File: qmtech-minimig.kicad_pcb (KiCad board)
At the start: 4 copper layers, 142.3 x 105.7 mm, 150 parts, among them IC1 ESP32-WROVER-B_(16MB), J1 DB9_Male, J10 DB23_Female_MountingHoles, J11 Conn_01x03_Male, J2 DB9_Male, J3 SCHA5B0200, J4 10118193-0001LF, J5 AUDIO-CONNECTOR-6P-SMD-344003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, J6 Mini-DIN-6, J7 Conn_02x13_Odd_Even, J8 Conn_01x04, J9 47151-0001, Q1 MMBT2222A, Q2 MMBT2222A, Q3 BSS84, SW1 SW_Push, U2 QM_XC7A35T_DDR3, U3 LT1963AxST-1.8, U4 INTERFACE-CP2102-GMR(QFN28), U5 MT3608, U6 TXS0108EPWR, U7 TXS0108EPWR

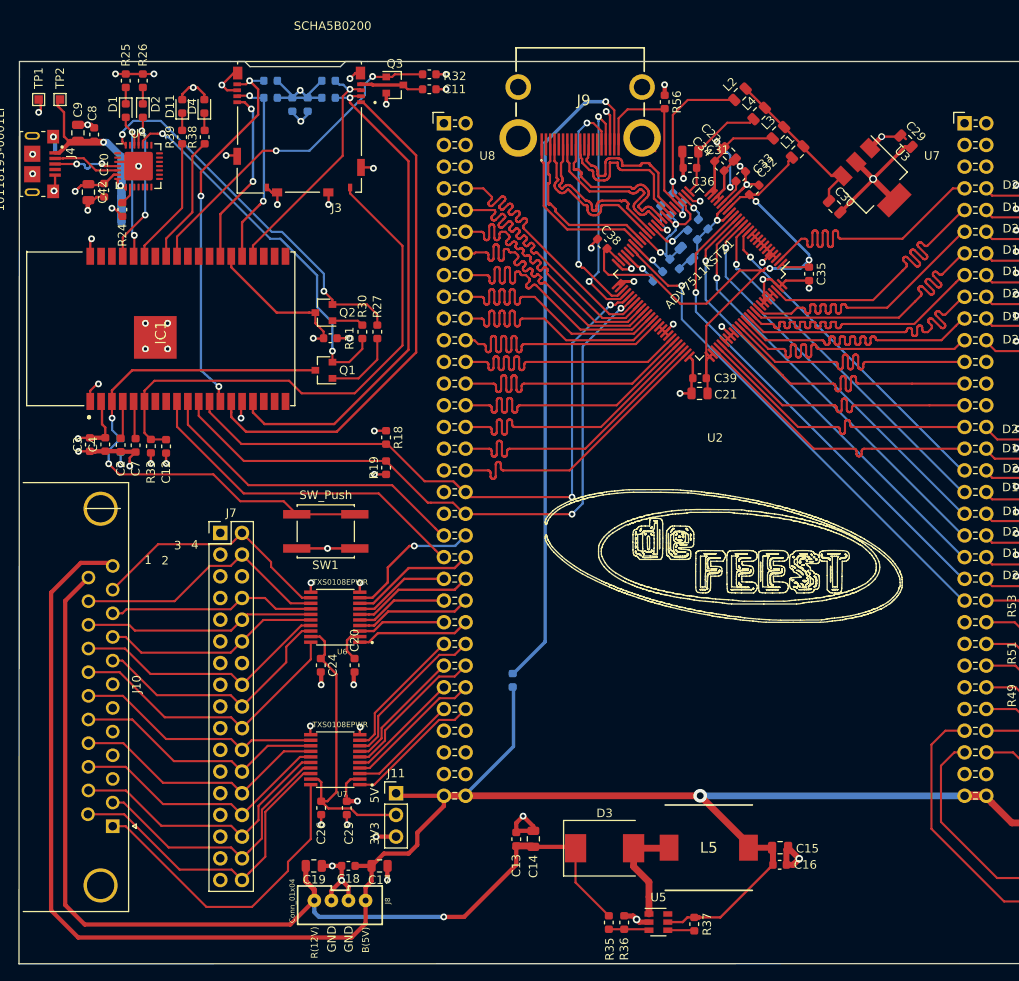
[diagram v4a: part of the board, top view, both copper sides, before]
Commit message: Fixed HDMI Impedance to 50Ohm, 100Ohm differential, for 0.1mm bord. Add pullups to HDMI I2C, connected DE pin to FPGA.
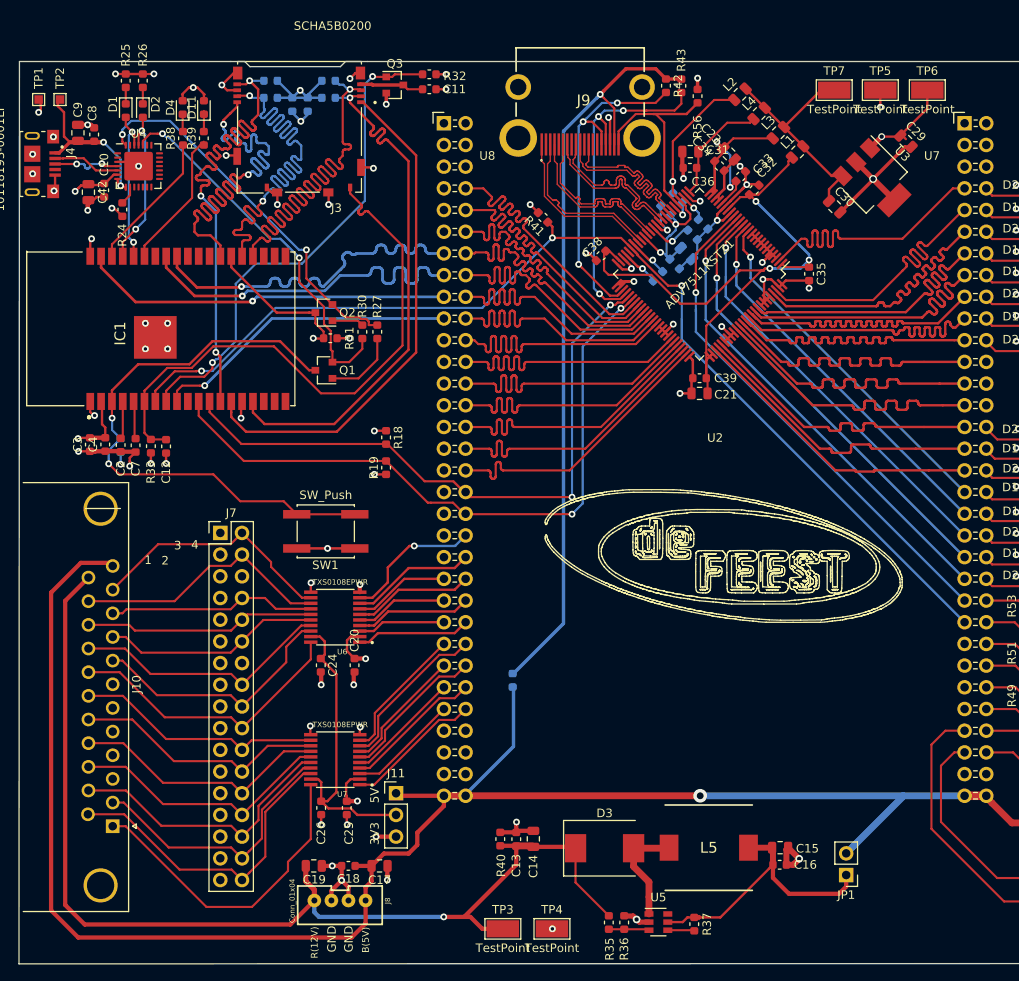
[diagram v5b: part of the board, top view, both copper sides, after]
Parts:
- added JP1: Jumper, Connector_PinHeader_2.54mm:PinHeader_1x02_P2.54mm_Vertical, F.Cu at (156.4, 140.5)
- added R40: 1M, Resistor_SMD:R_0603_1608Metric, F.Cu at (116.0, 136.3)
- added R41: 2K, Resistor_SMD:R_0603_1608Metric, F.Cu at (121.0, 63.5)
- added R42: 2k, Resistor_SMD:R_0603_1608Metric, F.Cu at (135.3, 48.1)
- added R43: 2k, Resistor_SMD:R_0603_1608Metric, F.Cu at (137.2, 48.1)
- added TP3: TestPoint, TestPoint:TestPoint_Keystone_5019_Minature, F.Cu at (116.2, 146.8)
- added TP4: TestPoint, TestPoint:TestPoint_Keystone_5019_Minature, F.Cu at (122.0, 146.8)
- added TP5: TestPoint, TestPoint:TestPoint_Keystone_5019_Minature, F.Cu at (160.4, 48.6)
- added TP6: TestPoint, TestPoint:TestPoint_Keystone_5019_Minature, F.Cu at (165.9, 48.6)
- added TP7: TestPoint, TestPoint:TestPoint_Keystone_5019_Minature, F.Cu at (155.1, 48.6)
- moved R56 3.91 mm to (139.1, 49.3)
- moved R38 2.54 mm to (78.8, 54.2)
- moved R39 2.54 mm to (81.2, 54.2)
- moved D11 2.54 mm to (81.2, 50.6)
- moved D4 2.54 mm to (78.8, 50.6)
- moved C38 1.41 mm to (127.8, 68.0), turned to 45 degrees
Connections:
- net STM_SPI1_CS renamed Net-(U2-PadU729)
- net STM_SPI1_MISO renamed Net-(U2-PadU723)
- net STM_SPI1_MOSI renamed Net-(U2-PadU721)
- net STM_SPI1_NSS renamed Net-(U2-PadU727)
- net STM_SPI1_SCK renamed Net-(U2-PadU725)
- net STM_USART1_CTS renamed Net-(U2-PadU79)
- net STM_USART1_RTS renamed Net-(U2-PadU77)
- net STM_USART1_RX renamed Net-(U2-PadU711)
- ADV7511KSTZ1 pad 97: GND -> ADV_DE
- C15 pad 1: VIN5V -> Net-(C15-Pad1)
- C16 pad 1: VIN5V -> Net-(C15-Pad1)
- IC1 pad 10: ESP_UART1_RX -> Net-(IC1-Pad10)
- IC1 pad 29: ADV_INT -> Net-(IC1-Pad29)
- IC1 pad 30: ESP_SD_VCC_EN -> ESP_VSPI_CLK
- IC1 pad 31: /MCU/LED1 -> ESP_VSPI_MISO
- IC1 pad 36: Net-(IC1-Pad36) -> /MCU/LED1
- IC1 pad 37: Net-(IC1-Pad37) -> ESP_VSPI_MOSI
- IC1 pad 7: Net-(IC1-Pad7) -> ADV_INT
- IC1 pad 8: Net-(IC1-Pad8) -> ESP_SD_VCC_EN
- IC1 pad 9: ESP_UART1_TX -> ESP_VSPI_CS
- L5 pad 2: VIN5V -> Net-(C15-Pad1)
- R37 pad 1: VIN5V -> Net-(C15-Pad1)
- U2 pad U713: STM_USART1_TX -> ESP_VSPI_CLK
- U2 pad U715: STM_USART1_CK -> ESP_VSPI_MISO
- U2 pad U717: STM_IO_34 -> ESP_VSPI_MOSI
- U2 pad U719: STM_IO_33 -> ESP_VSPI_CS
- U2 pad U739: ESP_UART1_RX -> Net-(U2-PadU739)
- U2 pad U741: ESP_UART1_TX -> Net-(U2-PadU741)
- U2 pad U811: ADV_B_0 -> ADV_DE
- U2 pad U813: ADV_B_1 -> ADV_B_0
- U2 pad U815: ADV_B_2 -> ADV_B_1
- U2 pad U817: ADV_B_3 -> ADV_B_2
- U2 pad U819: ADV_B_4 -> ADV_B_3
- U2 pad U821: ADV_B_5 -> ADV_B_4
- U2 pad U823: ADV_B_6 -> ADV_B_5
- U2 pad U825: ADV_B_7 -> ADV_B_6
- U2 pad U827: ADV_G_0 -> ADV_B_7
- U2 pad U829: ADV_CLK -> ADV_G_0
- U2 pad U831: ADV_G_1 -> ADV_CLK
- U2 pad U833: ADV_I2S0 -> ADV_G_1
- U2 pad U835: ADV_I2S1 -> ADV_I2S0
- U2 pad U837: ADV_I2S2 -> ADV_I2S1
- U2 pad U839: ADV_I2S3 -> ADV_I2S2
- U2 pad U841: ADV_SCLK -> ADV_I2S3
- U2 pad U843: ADV_LRCLK -> ADV_SCLK
- U2 pad U845: ADV_INT -> ADV_LRCLK
- U2 pad U847: Net-(U2-PadU847) -> ADV_INT
- U5 pad 5: VIN5V -> Net-(C15-Pad1)
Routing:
- net GND: track 262.6 -> 358.3 mm, vias 84 -> 86
- net ADV_INT: track 58.2 -> 127.9 mm, vias 1 -> 3
- net 3V3: track 124.7 -> 175.6 mm, vias 41 -> 43
- net ESP_VSPI_MOSI: track 0.00 -> 43.4 mm, vias 0 -> 1
- net ESP_VSPI_MISO: track 0.00 -> 43.1 mm, vias 0 -> 1
- net ESP_VSPI_CLK: track 0.00 -> 43.1 mm, vias 0 -> 1
- net ESP_SD_DATA0: track 22.9 -> 63.3 mm
- net ESP_UART1_TX: track 40.4 -> 0.00 mm
- net ESP_SD_DATA1: track 20.9 -> 60.0 mm
- net ESP_UART1_RX: track 37.9 -> 0.00 mm
- net ESP_VSPI_CS: track 0.00 -> 36.0 mm, vias 0 -> 1
- net ESP_SD_CMD: track 27.7 -> 63.5 mm
- net ADV_DE: track 0.00 -> 35.1 mm
- net Net-(C15-Pad1): track 0.00 -> 32.9 mm
- net ESP_SD_VCC_EN: track 39.7 -> 60.3 mm
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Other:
- net class HDMI: clearance 0.15 -> 0.2; trace_width 0.28 -> 0.16
- net class SPI_TOP added: clearance 0.15, trace_width 0.32, via_dia 0.8, via_drill 0.32

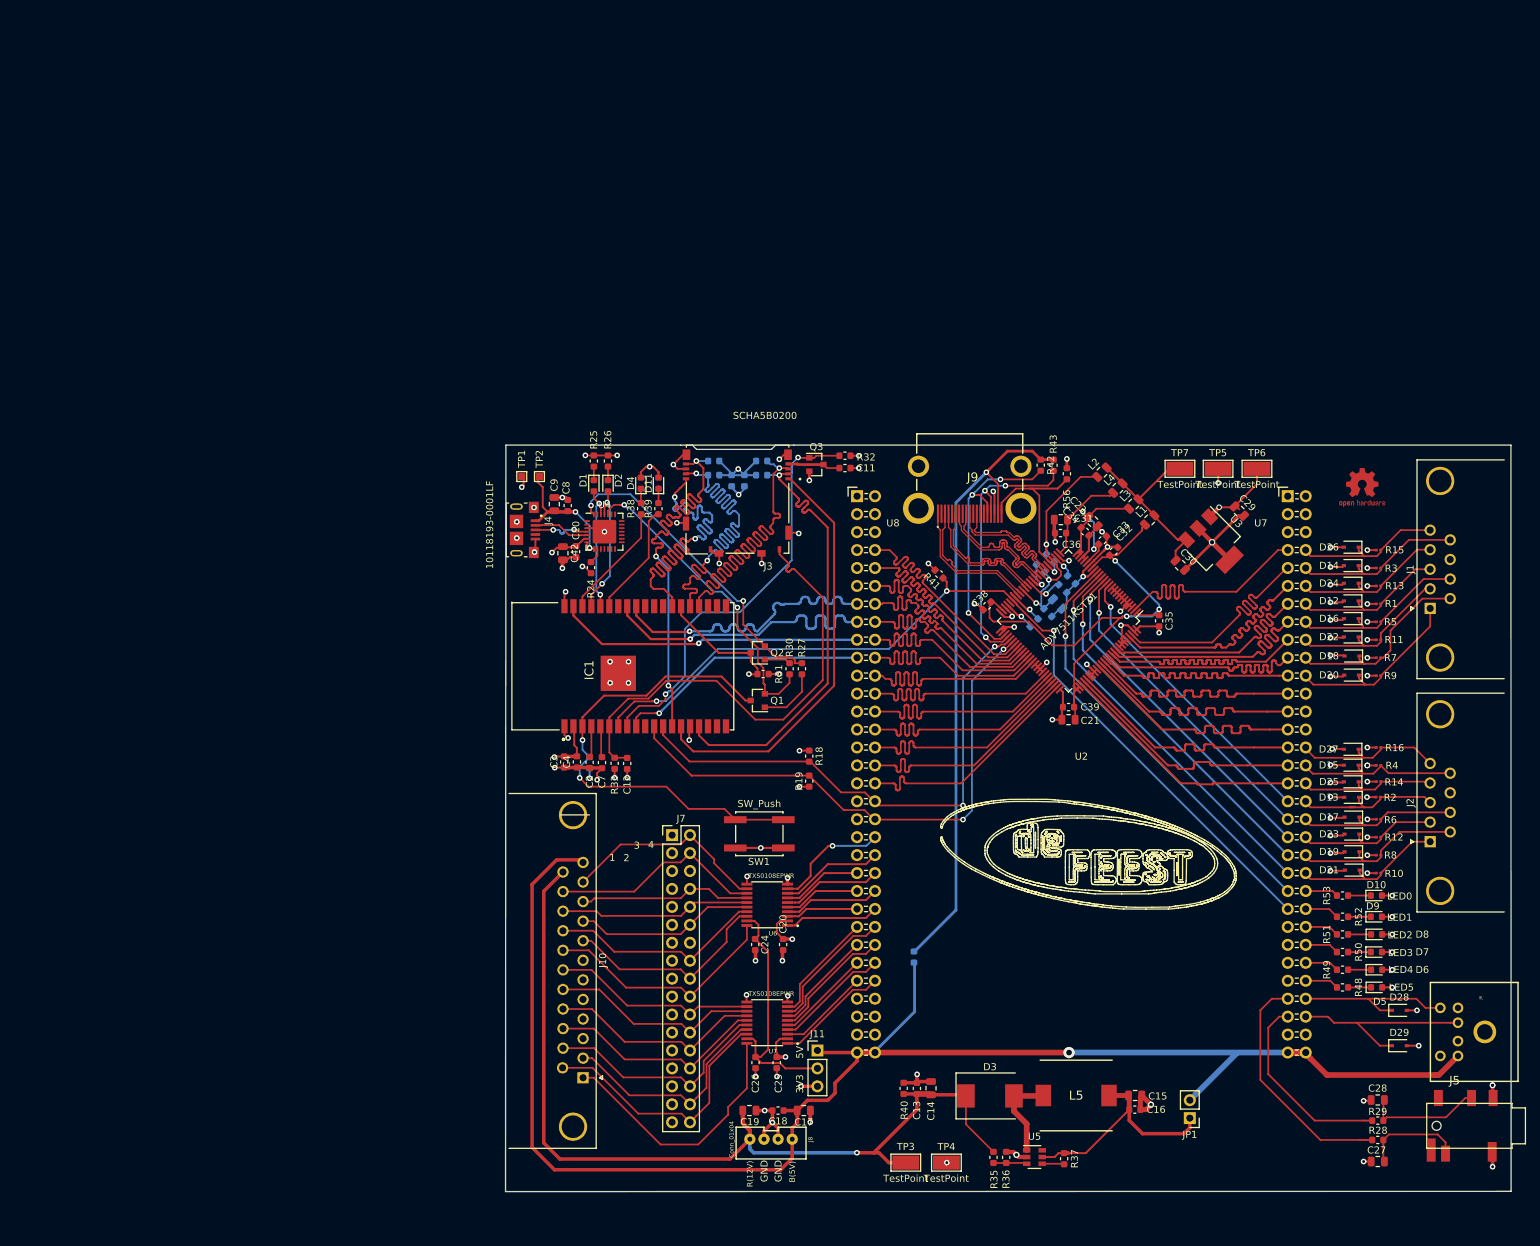
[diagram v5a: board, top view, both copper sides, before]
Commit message: Fixed some issues with the 50 Ohm impedance of the SPI lines. Added pinout .odt.
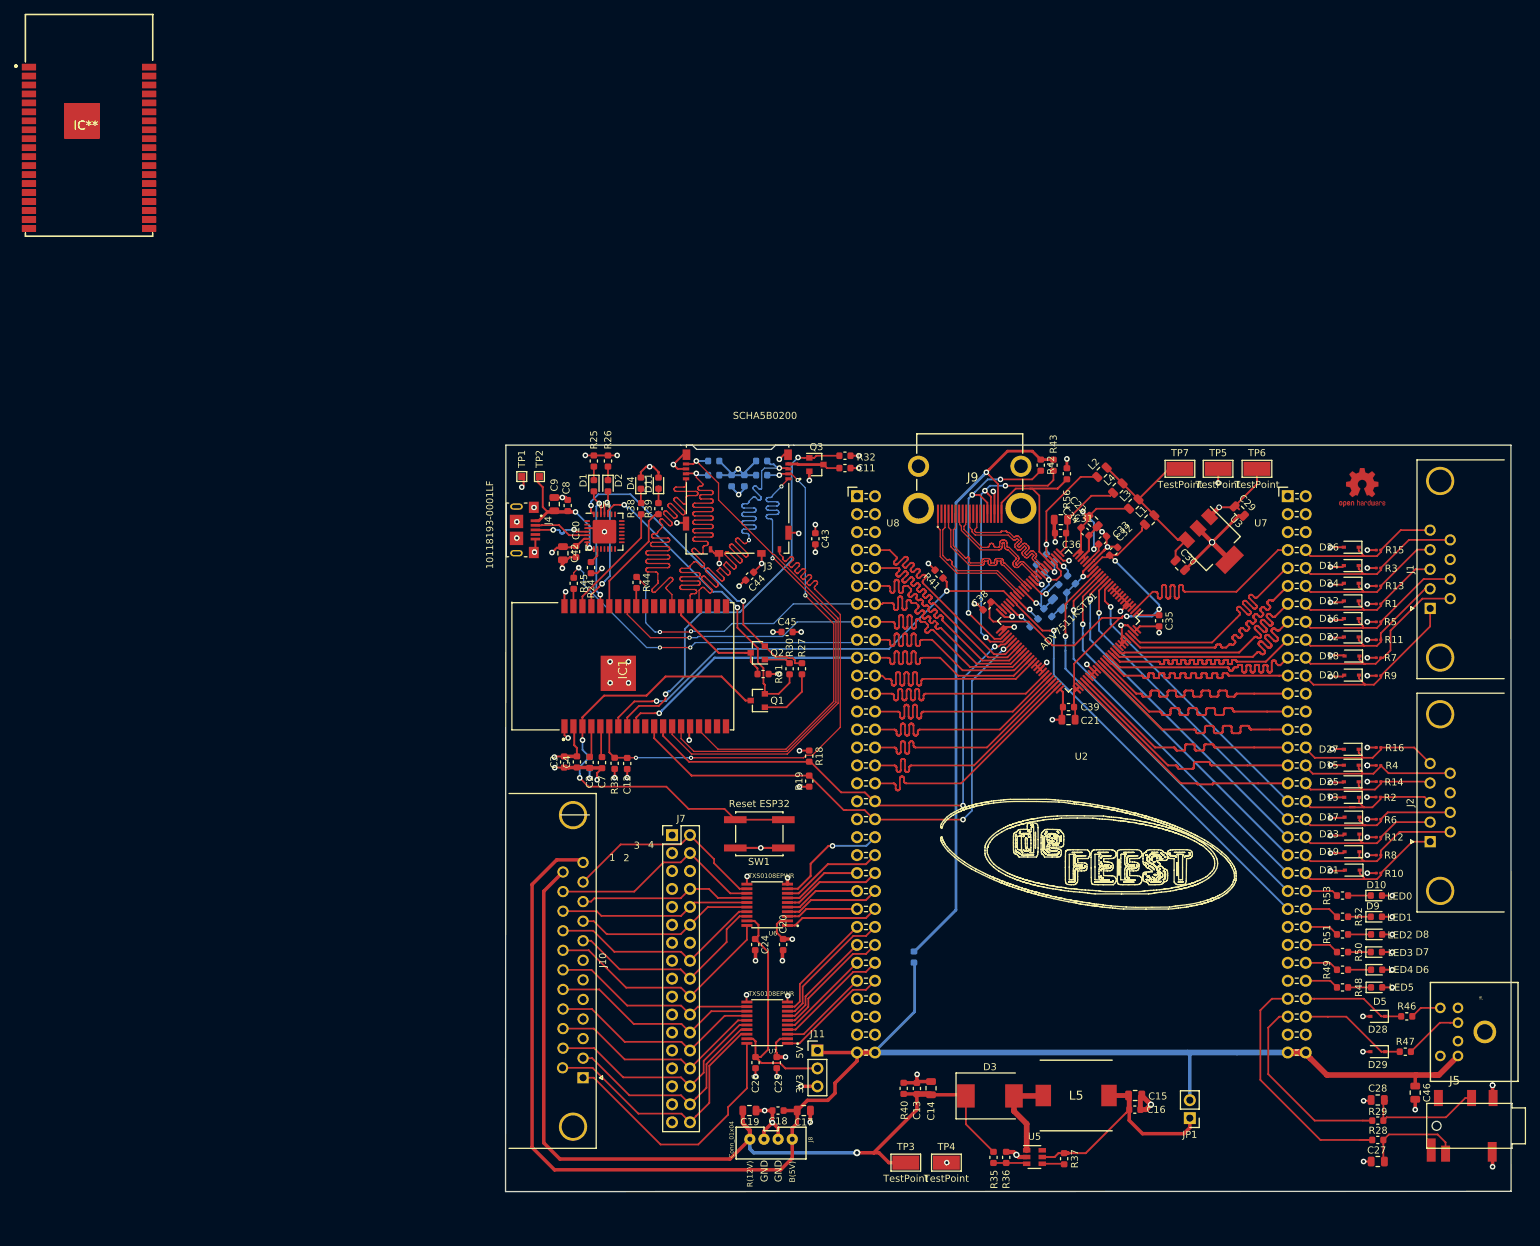
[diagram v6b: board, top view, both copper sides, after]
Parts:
- added C43: 10nF, Capacitor_SMD:C_0603_1608Metric, F.Cu at (103.5, 58.5)
- added C44: 10nF, Capacitor_SMD:C_0603_1608Metric, F.Cu at (94.2, 63.8)
- added C45: 10nF, Capacitor_SMD:C_0603_1608Metric, F.Cu at (99.5, 71.7)
- added C46: 10uF, Capacitor_SMD:C_0805_2012Metric, F.Cu at (188.3, 136.9)
- added IC** (x2): ESP32WROVERIB16MB, ESP32-WROVER-B_(16MB):ESP32WROVERIB16MB, F.Cu at (0.00, 0.00)
- added R44: 20, Resistor_SMD:R_0603_1608Metric, F.Cu at (78.2, 64.7)
- added R45: 20, Resistor_SMD:R_0603_1608Metric, F.Cu at (69.2, 64.8)
- added R46: 330, Resistor_SMD:R_0603_1608Metric, F.Cu at (187.2, 126.1)
- added R47: 330, Resistor_SMD:R_0603_1608Metric, F.Cu at (186.9, 131.1)
- SW1: value SW_Push -> Reset ESP32
- moved D28 3.17 mm to (183.1, 126.1), turned to 180 degrees
- moved D29 3.17 mm to (183.1, 131.1), turned to 180 degrees
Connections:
- IC1 pad 30: ESP_VSPI_CLK -> Net-(IC1-Pad30)
- IC1 pad 37: ESP_VSPI_MOSI -> Net-(IC1-Pad37)
- J6 pad 1: PS2_DAT1 -> Net-(J6-Pad1)
- J6 pad 5: PS2_CLK1 -> Net-(J6-Pad5)
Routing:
- net PS2_DAT1: track 28.4 -> 15.5 mm
- net ESP_SD_CLK: track 63.6 -> 75.0 mm, vias 3 -> 1
- net ESP_SD_CMD: track 63.5 -> 74.5 mm, vias 1 -> 2
- net ESP_SD_DATA1: track 60.0 -> 71.0 mm, vias 2 -> 0
- net ESP_SD_DATA0: track 63.3 -> 74.3 mm, vias 2 -> 1
- net ESP_SD_DATA2: track 60.1 -> 71.0 mm, vias 0 -> 2
- net ESP_SD_SW: track 67.2 -> 77.6 mm, vias 0 -> 2
- net PS2_CLK1: track 23.8 -> 14.5 mm
- net Net-(J6-Pad1): track 0.00 -> 8.37 mm
- net ESP_VSPI_MISO: track 43.1 -> 36.0 mm
- net GND: track 358.3 -> 363.0 mm, vias 86 -> 89
- net Net-(J6-Pad5): track 0.00 -> 4.46 mm
- net 3V3: track 175.6 -> 179.6 mm, vias 43 -> 46
- net ESP_VSPI_CLK: track 43.1 -> 39.1 mm, vias 1 -> 3
- net ESP_VSPI_MOSI: track 43.4 -> 47.2 mm, vias 1 -> 3
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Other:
- net class SPI_TOP: trace_width 0.32 -> 0.16; via_dia 0.8 -> 0.6; via_drill 0.32 -> 0.3

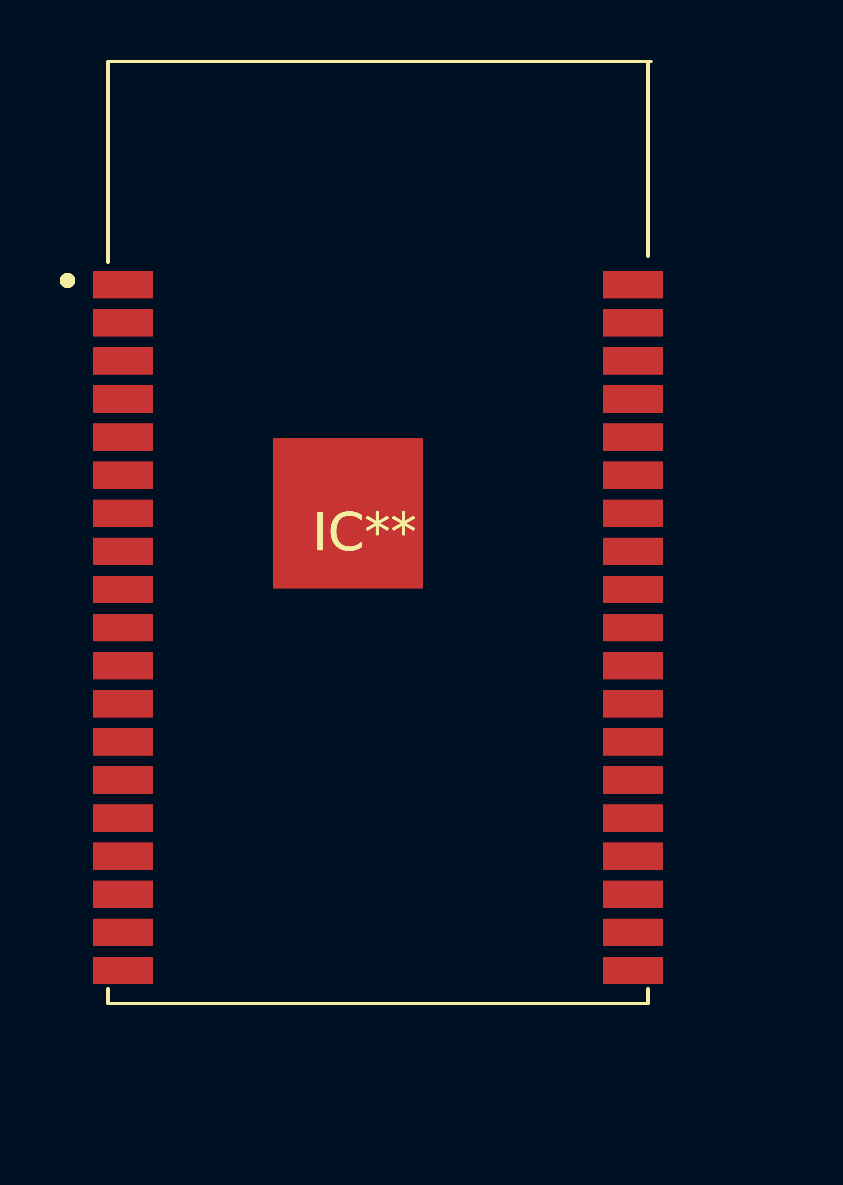
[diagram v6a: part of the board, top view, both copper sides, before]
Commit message: Removed an extra esp32 footprint that was outside of the design.
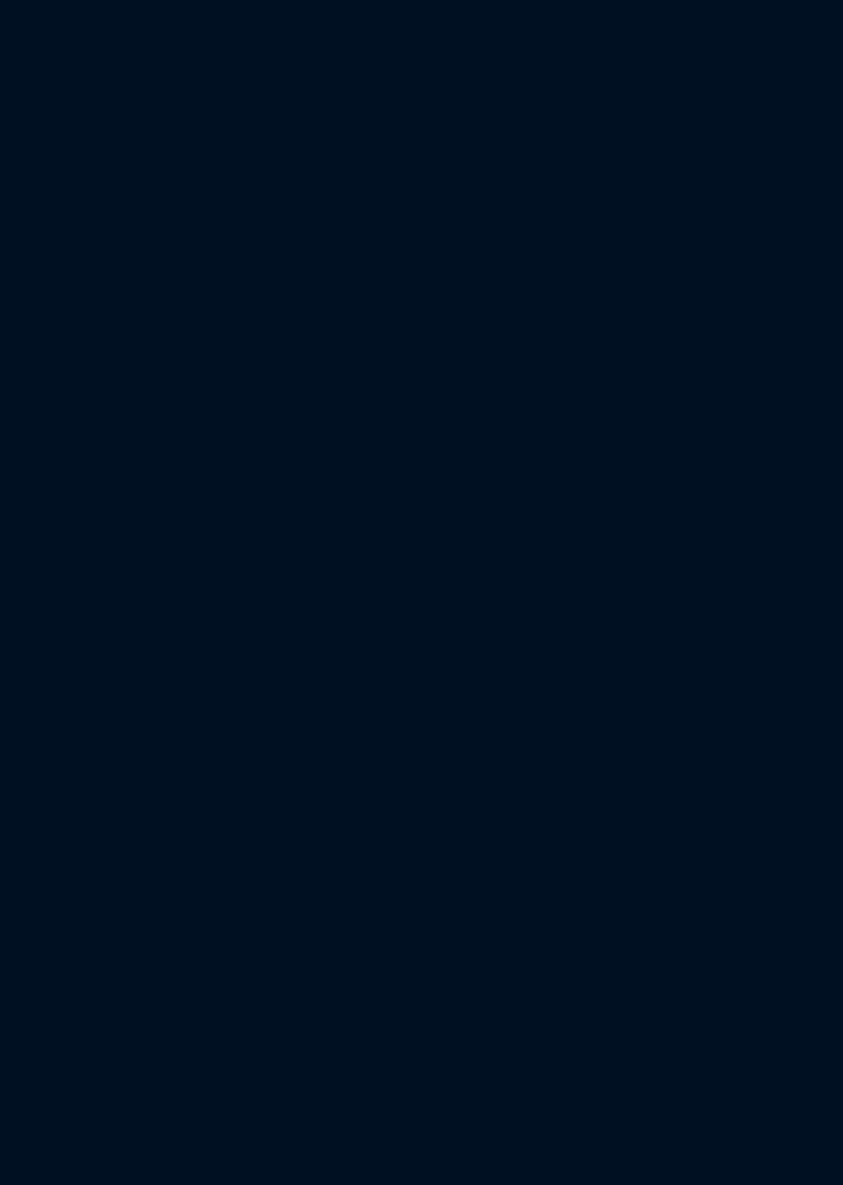
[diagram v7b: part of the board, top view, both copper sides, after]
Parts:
- removed IC** (x2): ESP32WROVERIB16MB, ESP32-WROVER-B_(16MB):ESP32WROVERIB16MB
